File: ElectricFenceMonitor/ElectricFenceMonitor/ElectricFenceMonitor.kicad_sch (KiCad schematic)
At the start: 17 parts, among them J3 Programming, J4 Ra01_Breakout_Module, Q1 BC548, U1 PICAXE-14M2, U2 PICAXE-18M2

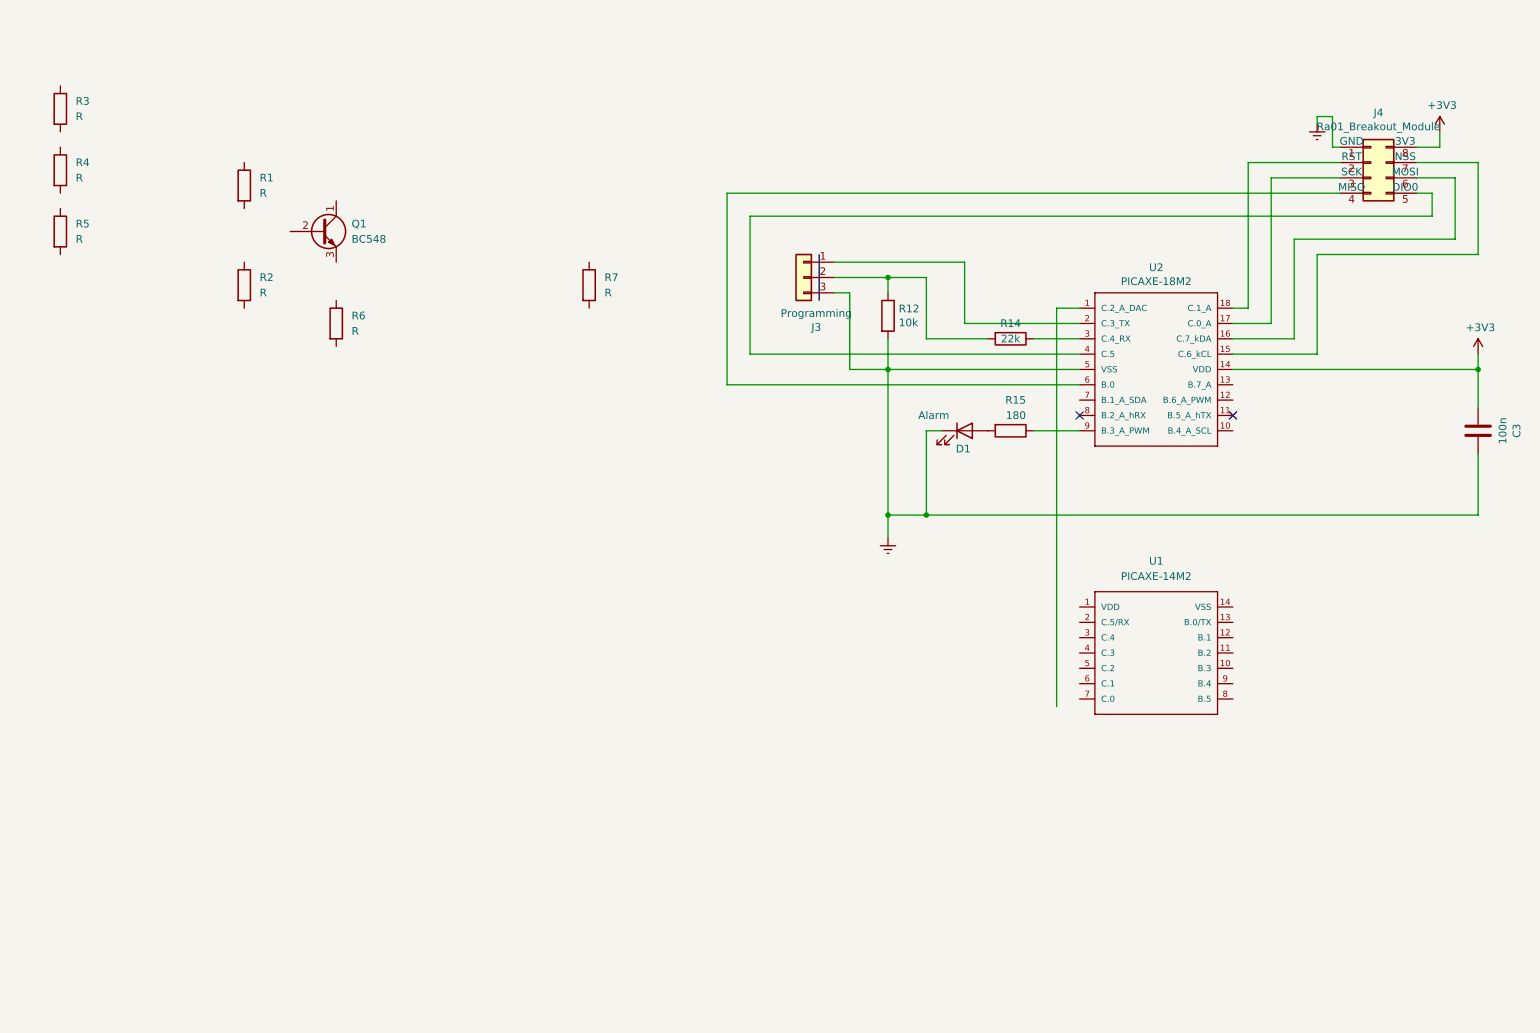
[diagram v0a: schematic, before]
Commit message: Electric fence layout planned
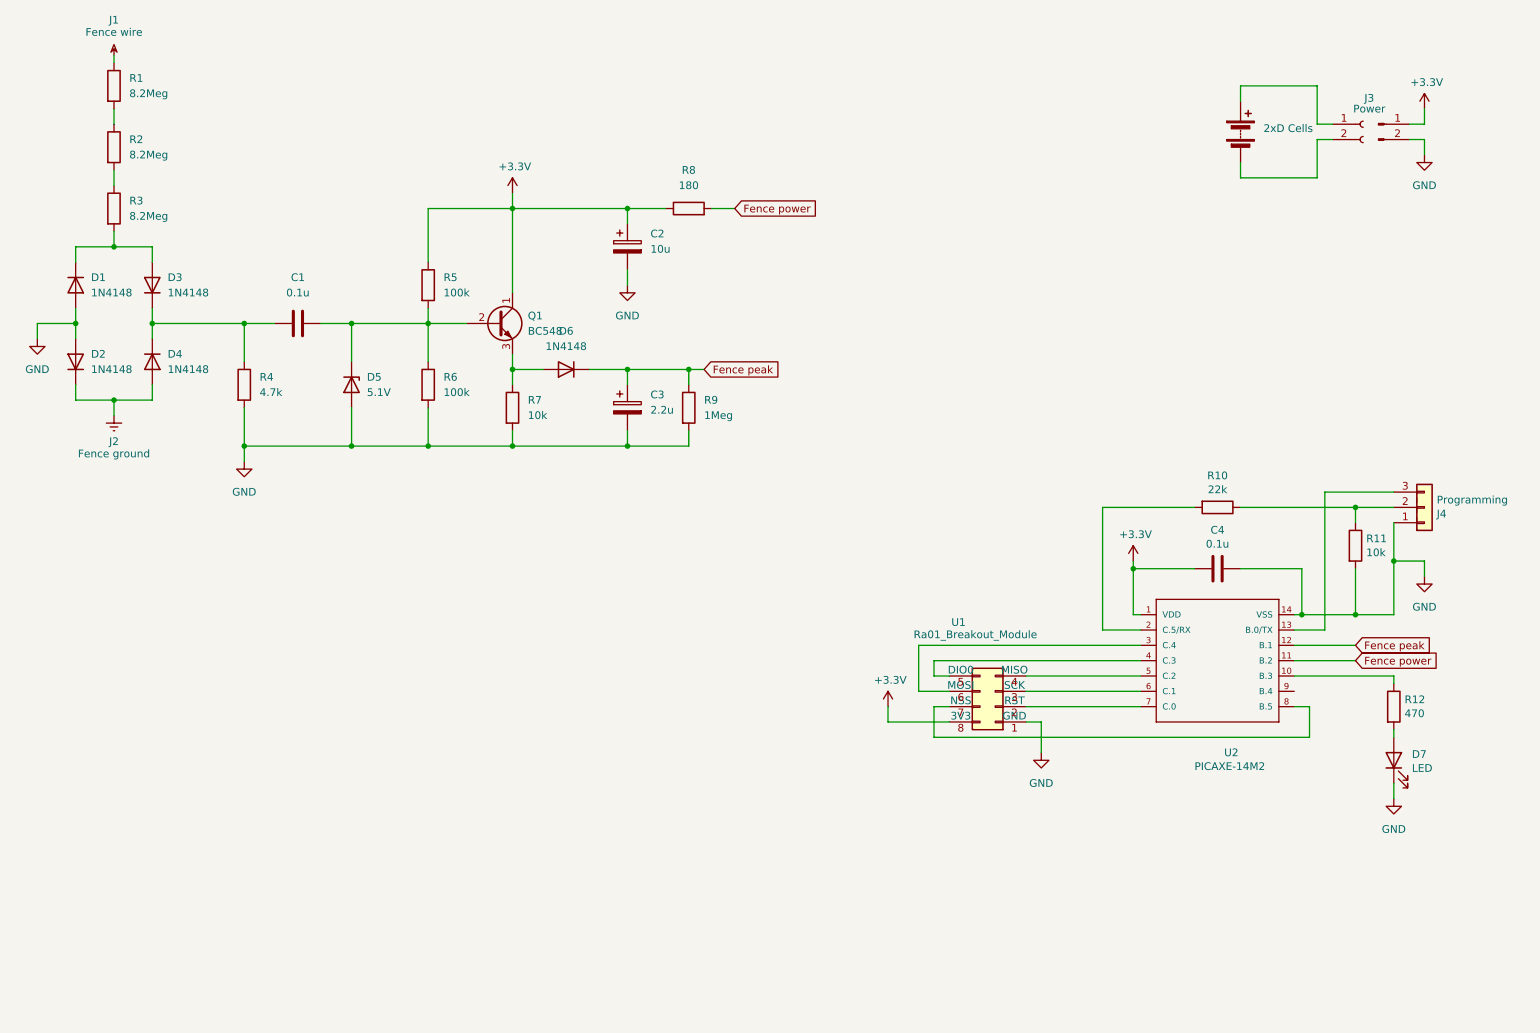
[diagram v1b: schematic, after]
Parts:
- removed C3: 100n, Capacitor_THT:C_Disc_D5.0mm_W2.5mm_P2.50mm, symbol Device:C
- removed D1: Alarm, LED_THT:LED_D5.0mm_Clear, symbol Device:LED
- removed J3: Programming, Connector_Molex:Molex_KK-254_AE-6410-03A_1x03_P2.54mm_Vertical, symbol Connector_Generic:Conn_01x03
- removed J4: Ra01_Breakout_Module, Package_DIP:DIP-8_W7.62mm_Socket, symbol PumpMonitor-rescue:Ra01_Breakout_Module-Ra01_Breakout_Module
- removed R14: 22k, Resistor_THT:R_Axial_DIN0207_L6.3mm_D2.5mm_P10.16mm_Horizontal, symbol Device:R
- removed R15: 180, Resistor_THT:R_Axial_DIN0207_L6.3mm_D2.5mm_P10.16mm_Horizontal, symbol Device:R
- removed U1: PICAXE-14M2, symbol picaxe-3:PICAXE-14M2
- removed U2: PICAXE-18M2, Package_DIP:DIP-18_W7.62mm_Socket, symbol PumpMonitor-rescue:PICAXE-18M2-Picaxe
- added #BT1: 2xD Cells, symbol Device:Battery
- added #J1: Conn_01x02_Socket, symbol Connector:Conn_01x02_Socket
- added C1: 0.1u, Capacitor_THT:C_Disc_D5.0mm_W2.5mm_P5.00mm, symbol Device:C
- added C2: 10u, Capacitor_THT:CP_Radial_D6.3mm_P2.50mm, symbol Device:C_Polarized
- added C3: 2.2u, Capacitor_THT:C_Axial_L5.1mm_D3.1mm_P10.00mm_Horizontal, symbol Device:C_Polarized
- added C4: 0.1u, Capacitor_THT:C_Rect_L9.0mm_W2.5mm_P7.50mm_MKT, symbol Device:C
- added D1, D4: 1N4148, Diode_THT:D_DO-35_SOD27_P10.16mm_Horizontal, symbol Diode:1N4148
- added D2: 1N4148, Diode_THT:D_DO-35_SOD27_P7.62mm_Horizontal, symbol Diode:1N4148
- added D3: 1N4148, Diode_THT:D_DO-35_SOD27_P12.70mm_Horizontal, symbol Diode:1N4148
- added D5: 5.1V, Diode_THT:D_A-405_P7.62mm_Horizontal, symbol Device:D_Zener
- added D6: 1N4148, Diode_THT:D_DO-35_SOD27_P5.08mm_Vertical_AnodeUp, symbol Diode:1N4148
- added D7: LED, LED_THT:LED_D5.0mm, symbol Device:LED
- added J1: Fence wire, MountingHole:MountingHole_3.5mm_Pad_Via, symbol power:HT
- added J2: Fence ground, MountingHole:MountingHole_3.5mm_Pad_Via, symbol power:GNDREF
- added J3: Power, TerminalBlock_Phoenix:TerminalBlock_Phoenix_MKDS-1,5-2-5.08_1x02_P5.08mm_Horizontal, symbol Connector:Conn_01x02_Pin
- added J4: Programming, Connector_Molex:Molex_KK-254_AE-6410-03A_1x03_P2.54mm_Vertical, symbol Connector_Generic:Conn_01x03
- added R1: 8.2Meg, Resistor_THT:R_Axial_DIN0617_L17.0mm_D6.0mm_P25.40mm_Horizontal, symbol Device:R
- added R10: 22k, Resistor_THT:R_Axial_DIN0207_L6.3mm_D2.5mm_P5.08mm_Vertical, symbol Device:R
- added R11: 10k, Resistor_THT:R_Axial_DIN0207_L6.3mm_D2.5mm_P2.54mm_Vertical, symbol Device:R
- added R8: 180, Resistor_THT:R_Axial_DIN0207_L6.3mm_D2.5mm_P15.24mm_Horizontal, symbol Device:R
- added U1: Ra01_Breakout_Module, Package_DIP:DIP-8_W7.62mm_Socket_LongPads, symbol Custom:Ra01_Breakout_Module-Ra01_Breakout_Module
- added U2: PICAXE-14M2, Package_DIP:DIP-14_W7.62mm_Socket_LongPads, symbol picaxe-3:PICAXE-14M2
- Q1: footprint Package_TO_SOT_THT:TO-92_Inline -> Package_TO_SOT_THT:TO-92_Inline_Wide
- R12: value 10k -> 470; footprint Resistor_THT:R_Axial_DIN0207_L6.3mm_D2.5mm_P10.16mm_Horizontal -> Resistor_THT:R_Axial_DIN0309_L9.0mm_D3.2mm_P25.40mm_Horizontal
- R2: renamed from R3; value R -> 8.2Meg; footprint (none) -> Resistor_THT:R_Axial_DIN0617_L17.0mm_D6.0mm_P25.40mm_Horizontal
- R3: renamed from R4; value R -> 8.2Meg; footprint (none) -> Resistor_THT:R_Axial_DIN0617_L17.0mm_D6.0mm_P25.40mm_Horizontal
- R4: renamed from R7; value R -> 4.7k; footprint (none) -> Resistor_THT:R_Axial_DIN0207_L6.3mm_D2.5mm_P2.54mm_Vertical
- R5: renamed from R1; value R -> 100k; footprint (none) -> Resistor_THT:R_Axial_DIN0207_L6.3mm_D2.5mm_P2.54mm_Vertical
- R6: renamed from R2; value R -> 100k; footprint (none) -> Resistor_THT:R_Axial_DIN0207_L6.3mm_D2.5mm_P7.62mm_Horizontal
- R7: renamed from R5; value R -> 10k; footprint (none) -> Resistor_THT:R_Axial_DIN0207_L6.3mm_D2.5mm_P7.62mm_Horizontal
- R9: renamed from R6; value R -> 1Meg; footprint (none) -> Resistor_THT:R_Axial_DIN0207_L6.3mm_D2.5mm_P10.16mm_Horizontal
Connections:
- net at R3.1: now also R2.2
- net at R3.2: now also D1.1 (K), D3.2 (A)
- net at R6.1: now also Q1.2 (B), R5.2, C1.2, D5.1 (K)
- net GND: now reaches R6.2
- net GND: now also R4.2, R7.2, R9.2, C2.2, C3.2, C4.1, D1.2 (A), D2.2 (A), D5.2 (A), D7.1 (K), J3.2 (Pin_2), J4.1 (Pin_1), R11.2, U1.1 (GND), U2.14 (VSS)
- net Fence peak: now reaches R9.1
- net Fence peak: now also C3.1, D6.1 (K), U2.12 (B.1)
- net +3.3V: now reaches Q1.1 (C)
- net +3.3V: now also R5.1, C2.1, C4.2, J3.1 (Pin_1), R8.1, U1.8 (3V3), U2.1 (VDD)
- net at Q1.3 (E): now also R7.1, D6.2 (A)
- net at R12.1: now also U2.10 (B.3)
- net at R2.1: now also R1.2
- net at R4.1: now also C1.1, D3.1 (K), D4.1 (K)
- net Earth: no longer names the net of R12.2
- net Earth: now also D7.2 (A)
- new net: D2.1 (K), D4.2 (A), J2.1
- new net: J4.2 (Pin_2), R10.1, R11.1
- new net: J4.3 (Pin_3), U2.13 (B.0/TX)
- new net: R10.2, U2.2 (C.5/RX)
- new net: U1.2 (RST), U2.7 (C.0)
- new net: U1.3 (SCK), U2.6 (C.1)
- new net: U1.4 (MISO), U2.5 (C.2)
- new net: U1.5 (DIO0), U2.4 (C.3)
- new net: U1.6 (MOSI), U2.3 (C.4)
- new net: U1.7 (NSS), U2.8 (B.5)
- new net: J1.1, R1.1
- new net: #BT1.1 (+), #J1.1 (Pin_1)
- new net: #BT1.2 (-), #J1.2 (Pin_2)
- new net Fence power: R8.2, U2.11 (B.2)
- no-connect marks 2 -> 0
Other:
- company: (none) -> Jotham Gates
- title: (none) -> Electric fence monitor
- moved on the sheet: Q1, R2, R3, R4, R5, R6, R7, R9

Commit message: Water baby layout, electric fence simulations
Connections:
- net +3.3V: no longer C2.1, Q1.1 (C), R5.1, R8.1
- new net: C2.1, Q1.1 (C), R5.1, R8.1
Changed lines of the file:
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@@
-	(wire
-		(pts
-			(xy 106.68 50.8) (xy 106.68 53.34)
-		)
-		(stroke
-			(width 0)
-			(type default)
-		)
-	)
 	(wire
 		(pts
@@
 					(unit 1)
 				)
-			)
-		)
-	)
-	(symbol
-		(lib_id "power:+3.3V")
-		(at 106.68 50.8 0)
-		(unit 1)
-		(exclude_from_sim no)
-		(in_bom yes)
-		(on_board yes)
-		(dnp no)
-		(property "Reference" "#PWR03"
-			(at 106.68 54.61 0)
-			(effects
-				(font
-					(size 1.27 1.27)
-				)
-				(hide yes)
-			)
-		)
-		(property "Value" "+3.3V"
-			(at 107.061 46.4058 0)
-			(effects
-				(font
-					(size 1.27 1.27)
-				)
-			)
-		)
-		(property "Footprint" ""
-			(at 106.68 50.8 0)
-			(effects
-				(font
-					(size 1.27 1.27)
-				)
-				(hide yes)
-			)
-		)
-		(property "Datasheet" ""
-			(at 106.68 50.8 0)
-			(effects
-				(font
-					(size 1.27 1.27)
-				)
-				(hide yes)
-			)
-		)
-		(property "Description" "Power symbol creates a global label with name \"+3.3V\""
-			(at 106.68 50.8 0)
-			(effects
-				(font
-					(size 1.27 1.27)
-				)
-				(hide yes)
-			)
-		)
-		(pin "1"
-		)
-		(instances
-			(project "ElectricFenceMonitor"
-				(path "/17c9612a-07a4-41df-91a9-f6c583bb55f9"
-					(reference "#PWR03")
-					(unit 1)
-				)
